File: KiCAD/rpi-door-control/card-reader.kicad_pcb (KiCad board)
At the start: 2 copper layers, 62 x 15 mm, 7 parts, among them J2 RJ45, P5 CONN_4, U2 BUZZER

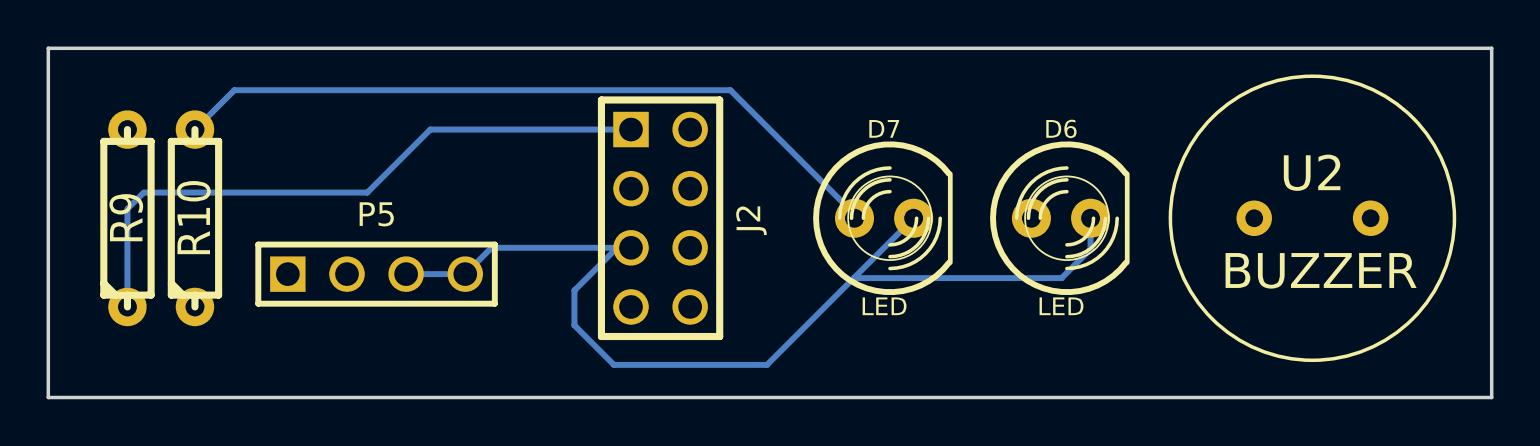
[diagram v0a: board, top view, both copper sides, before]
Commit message: cardreader board almost done, just need stupid buzzer to get connected in ratsnest
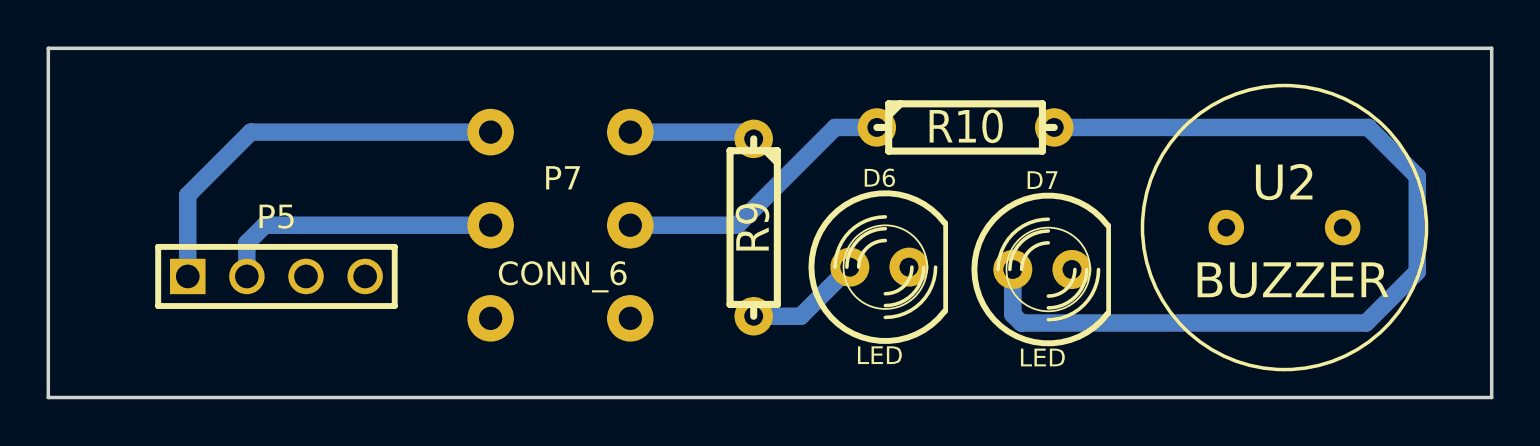
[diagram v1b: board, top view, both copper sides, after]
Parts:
- removed J2: RJ45, pin_array_4x2
- added P7: CONN_6, WIRE_HOLES_6, F.Cu at (103.7, 89.1)
- moved R10 33.3 mm to (121.1, 84.9), turned to 0 degrees
- moved R9 26.9 mm to (112.0, 89.2), turned to 270 degrees
- moved D6 8.08 mm to (117.4, 90.9)
- moved D7 7.15 mm to (124.4, 91.0)
- moved P5 4.30 mm to (91.5, 91.3)
- moved U2 1.26 mm to (134.8, 89.2)
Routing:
- net GND: track 44.7 -> 0.00 mm
- net /RED: track 27.3 -> 5.42 mm
- net +5V: track 0.00 -> 17.6 mm
- net /GREEN: track 0.00 -> 12.3 mm
- net /RFID TXD: track 0.00 -> 12.2 mm
- net N-0000010: track 31.4 -> 40.9 mm
- net N-0000011: track 0.00 -> 5.00 mm
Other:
- net class Default: clearance 0.254 -> 0.5; trace_width 0.254 -> 0.75
- rule trace_clearance: 0.254 -> 0.5

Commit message: board looks ok now, just need to fix bare_wire footprint
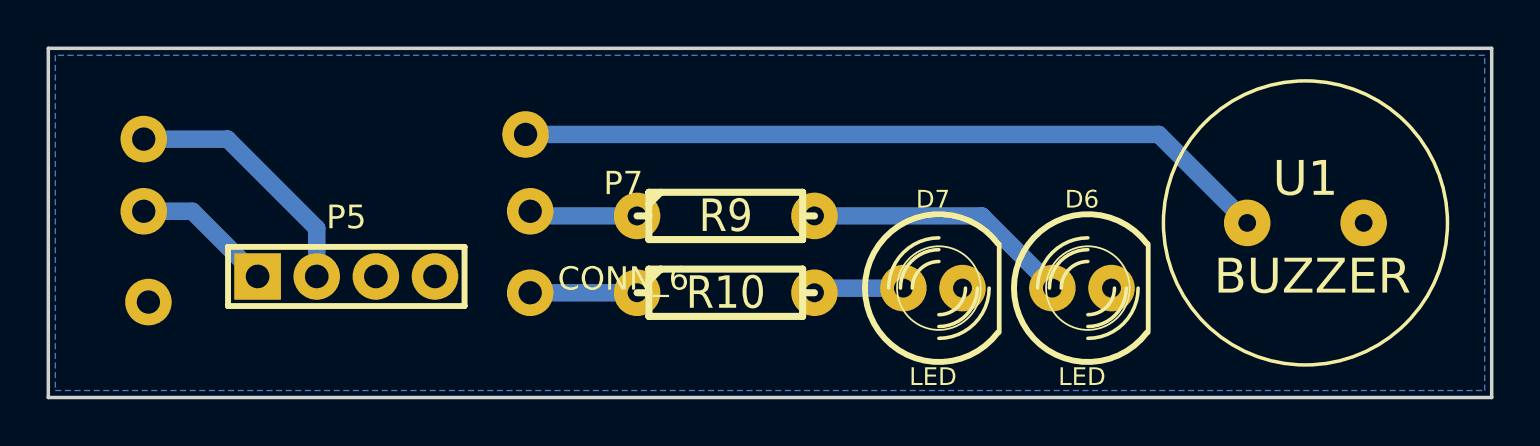
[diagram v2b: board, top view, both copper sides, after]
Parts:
- removed U2: BUZZER, BUZZER_SMALL
- added U1: BUZZER, BUZZER_SMALL, F.Cu at (135.7, 89.0)
- moved R10 12.5 mm to (110.8, 92.0)
- moved D6 8.75 mm to (126.1, 91.8)
- moved D7 4.77 mm to (119.7, 91.8)
- moved P5 3.00 mm to (94.5, 91.3)
- moved P7 2.61 mm to (106.3, 89.3)
- moved R9 1.30 mm to (110.8, 88.7), turned to 0 degrees
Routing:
- net N-0000010: track 40.9 -> 3.90 mm
- net /BELL: track 0.00 -> 32.6 mm
- net +5V: track 17.6 -> 6.05 mm
- net /GREEN: track 12.3 -> 4.59 mm
- net N-0000011: track 5.00 -> 11.5 mm
- net /RFID TXD: track 12.2 -> 11.1 mm
- net /RED: track 5.42 -> 4.67 mm
- added copper zone on B.Cu, net GND

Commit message: converted to smd pin headers for cardreader
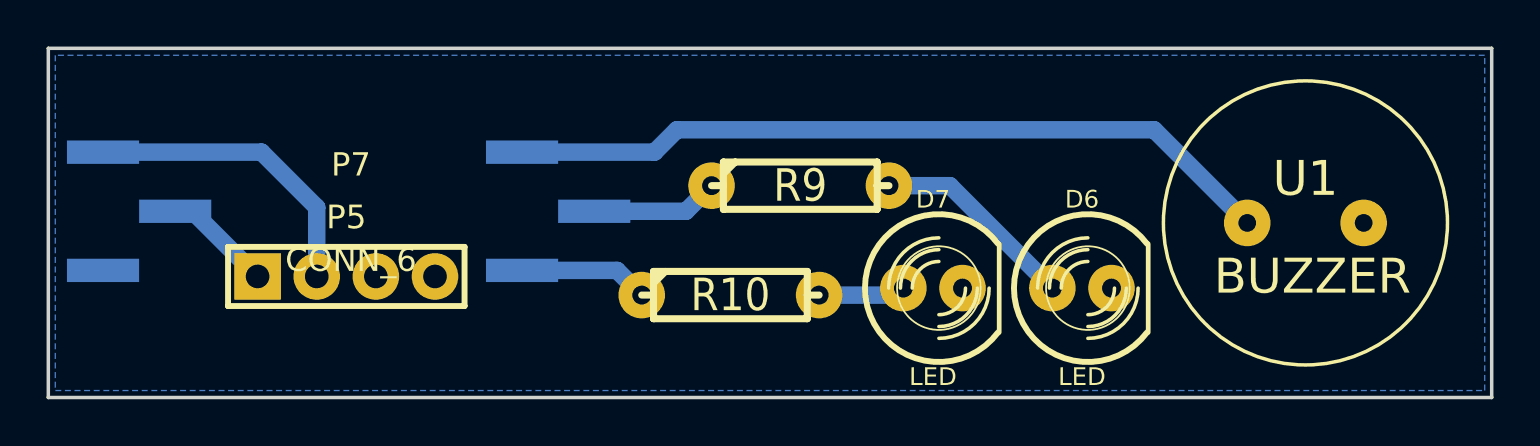
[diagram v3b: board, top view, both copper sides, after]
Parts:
- P7: footprint WIRE_HOLES_6 -> PINS_3x2_WIDE_SMD
- moved P7 11.7 mm to (94.6, 88.5)
- moved R9 3.45 mm to (114.0, 87.4)
- moved R10 0.22 mm to (111.0, 92.1)
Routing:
- net N-0000011: track 11.5 -> 8.84 mm
- net /RFID TXD: track 11.1 -> 13.1 mm
- net +5V: track 6.05 -> 4.70 mm
- net /GREEN: track 4.59 -> 5.58 mm
- net /RED: track 4.67 -> 5.50 mm
- net /BELL: track 32.6 -> 33.2 mm
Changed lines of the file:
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@@
     (thickness 1.6)
     (drawings 4)
-    (tracks 15)
+    (tracks 17)
     (zones 0)
     (modules 7)
@@
     (mod_text_size 1 1)
     (mod_text_width 0.15)
-    (pad_size 2 2)
-    (pad_drill 1.016)
+    (pad_size 3.1 1)
+    (pad_drill 0)
     (pad_to_mask_clearance 0)
     (aux_axis_origin 72.7 73.5)
@@
   )
   (module R3-LARGE_PADS (layer F.Cu)
-    (at 110.8 88.7)
+    (at 114 87.4)
     (descr "Resitance 3 pas")
     (tags R)
@@
   )
   (module R3-LARGE_PADS (layer F.Cu)
-    (at 110.8 92)
+    (at 111 92.1)
     (descr "Resitance 3 pas")
     (tags R)
@@
     )
   )
-  (module WIRE_HOLES_6 (layer F.Cu)
-    (at 106.3 89.3)
-    (fp_text reference P7 (at 0.1 -2) (layer F.SilkS)
-      (effects (font (size 1 1) (thickness 0.15)))
-    )
-    (fp_text value CONN_6 (at 0.1 2.1) (layer F.SilkS)
-      (effects (font (size 1 1) (thickness 0.15)))
-    )
-    (pad 1 thru_hole circle (at -20.5 -0.8) (size 2 2) (drill 1)
-      (layers *.Cu *.Mask F.SilkS)
-      (net 1 +5V)
-    )
-    (pad 2 thru_hole circle (at -3.9 -0.8) (size 2 2) (drill 1)
-      (layers *.Cu *.Mask F.SilkS)
-      (net 4 /RED)
-    )
-    (pad 4 thru_hole circle (at -20.5 -3.9) (size 2 2) (drill 1)
-      (layers *.Cu *.Mask F.SilkS)
-      (net 5 "/RFID TXD")
-    )
-    (pad 3 thru_hole circle (at -3.9 2.7) (size 2 2) (drill 1)
-      (layers *.Cu *.Mask F.SilkS)
-      (net 3 /GREEN)
-    )
-    (pad 6 thru_hole circle (at -20.3 3.1) (size 2 2) (drill 1)
-      (layers *.Cu *.Mask F.SilkS)
-      (net 6 GND)
-    )
-    (pad 5 thru_hole circle (at -4.1 -4.1) (size 2 2) (drill 1)
-      (layers *.Cu *.Mask F.SilkS)
-      (net 2 /BELL)
-    )
-  )
   (module BUZZER_SMALL (layer F.Cu)
     (at 135.7 89)
@@
     )
   )
+  (module PINS_3x2_WIDE_SMD (layer F.Cu)
+    (at 94.6 88.5)
+    (fp_text reference P7 (at 0.1 -2) (layer F.SilkS)
+      (effects (font (size 1 1) (thickness 0.15)))
+    )
+    (fp_text value CONN_6 (at 0.1 2.1) (layer F.SilkS)
+      (effects (font (size 1 1) (thickness 0.15)))
+    )
+    (pad 1 smd rect (at -7.45 0) (size 3.1 1)
+      (layers B.Cu B.Paste B.SilkS B.Mask)
+      (net 1 +5V)
+    )
+    (pad 2 smd rect (at 10.55 0) (size 3.1 1)
+      (layers B.Cu B.Paste B.SilkS B.Mask)
+      (net 4 /RED)
+    )
+    (pad 4 smd rect (at -10.55 -2.54) (size 3.1 1)
+      (layers B.Cu B.Paste B.SilkS B.Mask)
+      (net 5 "/RFID TXD")
+    )
+    (pad 3 smd rect (at 7.45 2.54) (size 3.1 1)
+      (layers B.Cu B.Paste B.SilkS B.Mask)
+      (net 3 /GREEN)
+    )
+    (pad 6 smd rect (at -10.55 2.54) (size 3.1 1)
+      (layers B.Cu B.Paste B.SilkS B.Mask)
+      (net 6 GND)
+    )
+    (pad 5 smd rect (at 7.45 -2.54) (size 3.1 1)
+      (layers B.Cu B.Paste B.SilkS B.Mask)
+      (net 2 /BELL)
+    )
+  )
   (gr_line (start 81.7 96.5) (end 81.7 81.5) (angle 90) (layer Edge.Cuts) (width 0.15))
   (gr_line (start 143.7 96.5) (end 81.7 96.5) (angle 90) (layer Edge.Cuts) (width 0.15))
   (gr_line (start 143.7 81.5) (end 143.7 96.5) (angle 90) (layer Edge.Cuts) (width 0.15))
   (gr_line (start 81.7 81.5) (end 143.7 81.5) (angle 90) (layer Edge.Cuts) (width 0.15))
-  (segment (start 85.8 88.5) (end 87.89 88.5) (width 0.75) (layer B.Cu) (net 1))
+  (segment (start 87.15 88.5) (end 87.89 88.5) (width 0.75) (layer B.Cu) (net 1))
   (segment (start 87.89 88.5) (end 90.69 91.3) (width 0.75) (layer B.Cu) (net 1))
-  (segment (start 102.2 85.2) (end 129.4 85.2) (width 0.75) (layer B.Cu) (net 2) (status 400000))
-  (segment (start 129.4 85.2) (end 133.2 89) (width 0.75) (layer B.Cu) (net 2) (status 800000))
-  (segment (start 106.99 92) (end 102.4 92) (width 0.75) (layer B.Cu) (net 3) (status C00000))
-  (segment (start 106.99 88.7) (end 102.6 88.7) (width 0.75) (layer B.Cu) (net 4) (status C00000))
-  (segment (start 102.6 88.7) (end 102.4 88.5) (width 0.75) (layer B.Cu) (net 4) (status C00000))
-  (segment (start 93.23 91.3) (end 93.23 89.23) (width 0.75) (layer B.Cu) (net 5))
-  (segment (start 89.4 85.4) (end 85.8 85.4) (width 0.75) (layer B.Cu) (net 5))
-  (segment (start 93.23 89.23) (end 89.4 85.4) (width 0.75) (layer B.Cu) (net 5))
-  (segment (start 118.43 91.8) (end 114.81 91.8) (width 0.75) (layer B.Cu) (net 7) (status C00000))
-  (segment (start 114.81 91.8) (end 114.61 92) (width 0.75) (layer B.Cu) (net 7) (status C00000))
-  (segment (start 124.83 91.8) (end 124.83 91.73) (width 0.75) (layer B.Cu) (net 8) (status C00000))
-  (segment (start 121.8 88.7) (end 114.61 88.7) (width 0.75) (layer B.Cu) (net 8) (status 800000))
-  (segment (start 124.83 91.73) (end 121.8 88.7) (width 0.75) (layer B.Cu) (net 8) (status 400000))
+  (segment (start 102.05 85.96) (end 107.74 85.96) (width 0.75) (layer B.Cu) (net 2) (status 400000))
+  (segment (start 129.2 85) (end 133.2 89) (width 0.75) (layer B.Cu) (net 2) (status 800000))
+  (segment (start 108.7 85) (end 129.2 85) (width 0.75) (layer B.Cu) (net 2))
+  (segment (start 107.74 85.96) (end 108.7 85) (width 0.75) (layer B.Cu) (net 2))
+  (segment (start 102.05 91.04) (end 106.13 91.04) (width 0.75) (layer B.Cu) (net 3) (status 400000))
+  (segment (start 106.13 91.04) (end 107.19 92.1) (width 0.75) (layer B.Cu) (net 3) (status 800000))
+  (segment (start 105.15 88.5) (end 109.09 88.5) (width 0.75) (layer B.Cu) (net 4) (status 400000))
+  (segment (start 109.09 88.5) (end 110.19 87.4) (width 0.75) (layer B.Cu) (net 4) (status 800000))
+  (segment (start 84.05 85.96) (end 90.86 85.96) (width 0.75) (layer B.Cu) (net 5))
+  (segment (start 93.23 88.33) (end 93.23 91.3) (width 0.75) (layer B.Cu) (net 5))
+  (segment (start 90.86 85.96) (end 93.23 88.33) (width 0.75) (layer B.Cu) (net 5))
+  (segment (start 114.81 92.1) (end 118.13 92.1) (width 0.75) (layer B.Cu) (net 7) (status C00000))
+  (segment (start 118.13 92.1) (end 118.43 91.8) (width 0.75) (layer B.Cu) (net 7) (status C00000))
+  (segment (start 117.81 87.4) (end 120.43 87.4) (width 0.75) (layer B.Cu) (net 8) (status 400000))
+  (segment (start 120.43 87.4) (end 124.83 91.8) (width 0.75) (layer B.Cu) (net 8) (status 800000))
   (zone (net 6) (net_name GND) (layer B.Cu) (hatch edge 0.508)
     (connect_pads (clearance 1))

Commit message: Tweaked footprints for smd header pins on card reader
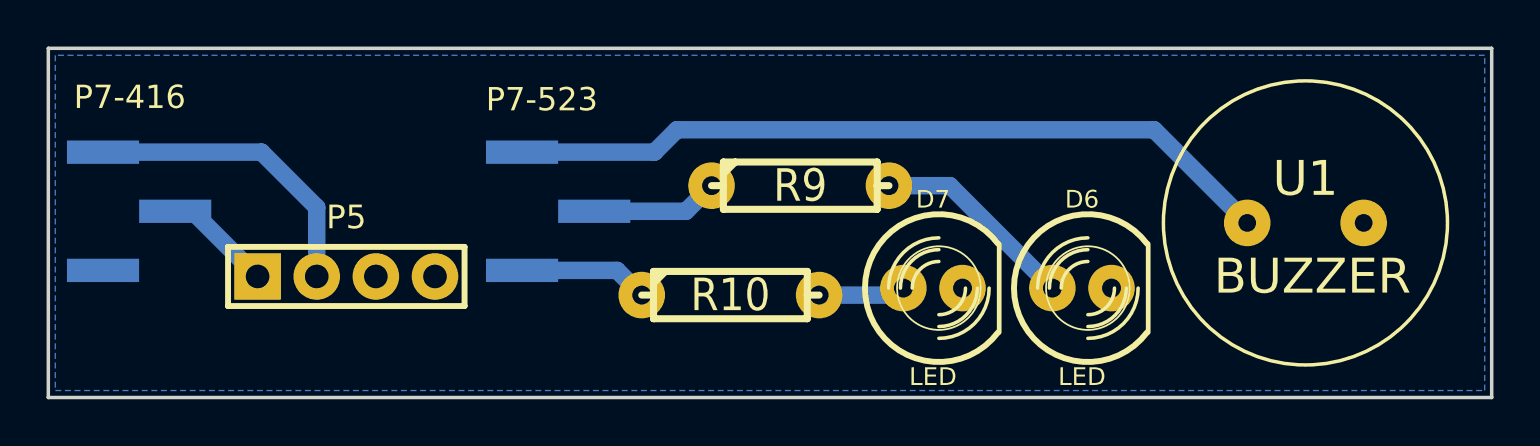
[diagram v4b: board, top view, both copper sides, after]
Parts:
- renumbered P7 to P7-416
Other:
- board text added: "P7-523"
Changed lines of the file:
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@@
     (links 12)
     (no_connects 1)
-    (area 81.624999 81.424999 143.775001 96.575001)
+    (area 81.291667 81.424999 143.775001 96.575001)
     (thickness 1.6)
-    (drawings 4)
+    (drawings 5)
     (tracks 17)
     (zones 0)
@@
   (title_block
     (title "Card Reader Board")
-    (rev 0.3)
+    (rev 0.3.1)
     (company SBW)
     (comment 1 "To be used with Parallax serial RFID reader")
@@
     (visible_elements 7FFFFFFF)
     (pcbplotparams
-      (layerselection 3178497)
-      (usegerberextensions true)
+      (layerselection 2097152)
+      (usegerberextensions false)
       (excludeedgelayer true)
       (linewidth 0.100000)
@@
       (padsonsilk false)
       (subtractmaskfromsilk false)
-      (outputformat 1)
+      (outputformat 2)
       (mirror false)
-      (drillshape 1)
+      (drillshape 0)
       (scaleselection 1)
-      (outputdirectory ""))
+      (outputdirectory Terry/))
   )
   (net 0 "")
@@
   (module PINS_3x2_WIDE_SMD (layer F.Cu)
     (at 94.6 88.5)
-    (fp_text reference P7 (at 0.1 -2) (layer F.SilkS)
+    (fp_text reference P7-416 (at -9.4 -4.9) (layer F.SilkS)
       (effects (font (size 1 1) (thickness 0.15)))
     )
-    (fp_text value CONN_6 (at 0.1 2.1) (layer F.SilkS)
+    (fp_text value CONN_6 (at 0.1 -4.8) (layer F.SilkS) hide
       (effects (font (size 1 1) (thickness 0.15)))
     )
@@
       (net 2 /BELL)
     )
+  )
+  (gr_text P7-523 (at 102.9 83.7) (layer F.SilkS)
+    (effects (font (size 1 1) (thickness 0.15)))
   )
   (gr_line (start 81.7 96.5) (end 81.7 81.5) (angle 90) (layer Edge.Cuts) (width 0.15))
@@
   (segment (start 87.15 88.5) (end 87.89 88.5) (width 0.75) (layer B.Cu) (net 1))
   (segment (start 87.89 88.5) (end 90.69 91.3) (width 0.75) (layer B.Cu) (net 1))
-  (segment (start 102.05 85.96) (end 107.74 85.96) (width 0.75) (layer B.Cu) (net 2) (status 400000))
-  (segment (start 129.2 85) (end 133.2 89) (width 0.75) (layer B.Cu) (net 2) (status 800000))
+  (segment (start 102.05 85.96) (end 107.74 85.96) (width 0.75) (layer B.Cu) (net 2))
+  (segment (start 129.2 85) (end 133.2 89) (width 0.75) (layer B.Cu) (net 2))
   (segment (start 108.7 85) (end 129.2 85) (width 0.75) (layer B.Cu) (net 2))
   (segment (start 107.74 85.96) (end 108.7 85) (width 0.75) (layer B.Cu) (net 2))
-  (segment (start 102.05 91.04) (end 106.13 91.04) (width 0.75) (layer B.Cu) (net 3) (status 400000))
-  (segment (start 106.13 91.04) (end 107.19 92.1) (width 0.75) (layer B.Cu) (net 3) (status 800000))
-  (segment (start 105.15 88.5) (end 109.09 88.5) (width 0.75) (layer B.Cu) (net 4) (status 400000))
-  (segment (start 109.09 88.5) (end 110.19 87.4) (width 0.75) (layer B.Cu) (net 4) (status 800000))
+  (segment (start 102.05 91.04) (end 106.13 91.04) (width 0.75) (layer B.Cu) (net 3))
+  (segment (start 106.13 91.04) (end 107.19 92.1) (width 0.75) (layer B.Cu) (net 3))
+  (segment (start 105.15 88.5) (end 109.09 88.5) (width 0.75) (layer B.Cu) (net 4))
+  (segment (start 109.09 88.5) (end 110.19 87.4) (width 0.75) (layer B.Cu) (net 4))
   (segment (start 84.05 85.96) (end 90.86 85.96) (width 0.75) (layer B.Cu) (net 5))
   (segment (start 93.23 88.33) (end 93.23 91.3) (width 0.75) (layer B.Cu) (net 5))
   (segment (start 90.86 85.96) (end 93.23 88.33) (width 0.75) (layer B.Cu) (net 5))
-  (segment (start 114.81 92.1) (end 118.13 92.1) (width 0.75) (layer B.Cu) (net 7) (status C00000))
-  (segment (start 118.13 92.1) (end 118.43 91.8) (width 0.75) (layer B.Cu) (net 7) (status C00000))
-  (segment (start 117.81 87.4) (end 120.43 87.4) (width 0.75) (layer B.Cu) (net 8) (status 400000))
-  (segment (start 120.43 87.4) (end 124.83 91.8) (width 0.75) (layer B.Cu) (net 8) (status 800000))
+  (segment (start 114.81 92.1) (end 118.13 92.1) (width 0.75) (layer B.Cu) (net 7))
+  (segment (start 118.13 92.1) (end 118.43 91.8) (width 0.75) (layer B.Cu) (net 7))
+  (segment (start 117.81 87.4) (end 120.43 87.4) (width 0.75) (layer B.Cu) (net 8))
+  (segment (start 120.43 87.4) (end 124.83 91.8) (width 0.75) (layer B.Cu) (net 8))
   (zone (net 6) (net_name GND) (layer B.Cu) (hatch edge 0.508)
     (connect_pads (clearance 1))
